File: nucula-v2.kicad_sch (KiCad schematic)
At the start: 7 parts, among them J4 MAIN LINK / OPTIONAL, U9 MCP1700T-3002E/TT

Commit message: Prepare components and JLCPCB BOM for 10-board assembly
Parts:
- C49: LCSC (none) -> C28323; MPN (none) -> CL21B105KBFNNNE; Manufacturer (none) -> Samsung Electro-Mechanics; Tolerance 20% -> 10%; Voltage 10 V -> 50 V
- C50: LCSC (none) -> C19110; MPN (none) -> CL21B225KAFNNNE; Manufacturer (none) -> Samsung Electro-Mechanics; Tolerance 20% -> 10%; Voltage 10 V -> 25 V
- R19, R20: LCSC (none) -> C4190; MPN (none) -> 0603WAF2201T5E; Manufacturer (none) -> UNI-ROYAL(Uniroyal Elec)
- R40: LCSC (none) -> C25803; MPN (none) -> 0603WAF1003T5E; Manufacturer (none) -> UNI-ROYAL(Uniroyal Elec)
- U9: LCSC (none) -> C62244; Manufacturer Microchip -> Microchip Tech
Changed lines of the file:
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@@
       )
     )
-    (property "Manufacturer" "Microchip"
+    (property "Manufacturer" "Microchip Tech"
       (at 66.04 139.7 0)
       (effects
@@
           (unit 1)
         )
+      )
+    )
+    (property "LCSC" "C62244"
+      (at 66.04 139.7 0)
+      (effects
+        (font
+          (size 1.0 1.0)
+        )
+        (hide yes)
       )
     )
@@
       )
     )
-    (property "Datasheet" ""
+    (property "Datasheet" "https://www.lcsc.com/datasheet/lcsc_datasheet_2304140030_Samsung-Electro-Mechanics-CL21B105KBFNNNE_C28323.pdf"
       (at 35.56 160.02 0)
       (effects
@@
       )
     )
-    (property "Voltage" "10 V"
+    (property "Voltage" "50 V"
       (at 35.56 160.02 0)
       (effects
@@
       )
     )
-    (property "Tolerance" "20%"
+    (property "Tolerance" "10%"
       (at 35.56 160.02 0)
       (effects
@@
           (unit 1)
         )
+      )
+    )
+    (property "Manufacturer" "Samsung Electro-Mechanics"
+      (at 35.56 160.02 0)
+      (effects
+        (font
+          (size 1.0 1.0)
+        )
+        (hide yes)
+      )
+    )
+    (property "MPN" "CL21B105KBFNNNE"
+      (at 35.56 160.02 0)
+      (effects
+        (font
+          (size 1.0 1.0)
+        )
+        (hide yes)
+      )
+    )
+    (property "LCSC" "C28323"
+      (at 35.56 160.02 0)
+      (effects
+        (font
+          (size 1.0 1.0)
+        )
+        (hide yes)
       )
     )
@@
       )
     )
-    (property "Datasheet" ""
+    (property "Datasheet" "https://www.lcsc.com/datasheet/lcsc_datasheet_2304140030_Samsung-Electro-Mechanics-CL21B225KAFNNNE_C19110.pdf"
       (at 96.52 160.02 0)
       (effects
@@
       )
     )
-    (property "Voltage" "10 V"
+    (property "Voltage" "25 V"
       (at 96.52 160.02 0)
       (effects
@@
       )
     )
-    (property "Tolerance" "20%"
+    (property "Tolerance" "10%"
       (at 96.52 160.02 0)
       (effects
@@
           (unit 1)
         )
+      )
+    )
+    (property "Manufacturer" "Samsung Electro-Mechanics"
+      (at 96.52 160.02 0)
+      (effects
+        (font
+          (size 1.0 1.0)
+        )
+        (hide yes)
+      )
+    )
+    (property "MPN" "CL21B225KAFNNNE"
+      (at 96.52 160.02 0)
+      (effects
+        (font
+          (size 1.0 1.0)
+        )
+        (hide yes)
+      )
+    )
+    (property "LCSC" "C19110"
+      (at 96.52 160.02 0)
+      (effects
+        (font
+          (size 1.0 1.0)
+        )
+        (hide yes)
       )
     )
@@
       )
     )
-    (property "Datasheet" ""
+    (property "Datasheet" "https://www.lcsc.com/datasheet/lcsc_datasheet_2206010230_UNI-ROYAL-Uniroyal-Elec-0603WAF2201T5E_C4190.pdf"
       (at 142.24 138.43 0)
       (effects
@@
           (unit 1)
         )
+      )
+    )
+    (property "Manufacturer" "UNI-ROYAL(Uniroyal Elec)"
+      (at 142.24 138.43 0)
+      (effects
+        (font
+          (size 1.0 1.0)
+        )
+        (hide yes)
+      )
+    )
+    (property "MPN" "0603WAF2201T5E"
+      (at 142.24 138.43 0)
+      (effects
+        (font
+          (size 1.0 1.0)
+        )
+        (hide yes)
+      )
+    )
+    (property "LCSC" "C4190"
+      (at 142.24 138.43 0)
+      (effects
+        (font
+          (size 1.0 1.0)
+        )
+        (hide yes)
       )
     )
@@
       )
     )
-    (property "Datasheet" ""
+    (property "Datasheet" "https://www.lcsc.com/datasheet/lcsc_datasheet_2206010230_UNI-ROYAL-Uniroyal-Elec-0603WAF2201T5E_C4190.pdf"
       (at 175.26 138.43 0)
       (effects
@@
           (unit 1)
         )
+      )
+    )
+    (property "Manufacturer" "UNI-ROYAL(Uniroyal Elec)"
+      (at 175.26 138.43 0)
+      (effects
+        (font
+          (size 1.0 1.0)
+        )
+        (hide yes)
+      )
+    )
+    (property "MPN" "0603WAF2201T5E"
+      (at 175.26 138.43 0)
+      (effects
+        (font
+          (size 1.0 1.0)
+        )
+        (hide yes)
+      )
+    )
+    (property "LCSC" "C4190"
+      (at 175.26 138.43 0)
+      (effects
+        (font
+          (size 1.0 1.0)
+        )
+        (hide yes)
       )
     )
@@
       )
     )
-    (property "Datasheet" ""
+    (property "Datasheet" "https://www.lcsc.com/datasheet/lcsc_datasheet_2206010045_UNI-ROYAL-Uniroyal-Elec-0603WAF1003T5E_C25803.pdf"
       (at 175.26 172.72 0)
       (effects
@@
       )
     )
+    (property "Manufacturer" "UNI-ROYAL(Uniroyal Elec)"
+      (at 175.26 172.72 0)
+      (effects
+        (font
+          (size 1.0 1.0)
+        )
+        (hide yes)
+      )
+    )
+    (property "MPN" "0603WAF1003T5E"
+      (at 175.26 172.72 0)
+      (effects
+        (font
+          (size 1.0 1.0)
+        )
+        (hide yes)
+      )
+    )
+    (property "LCSC" "C25803"
+      (at 175.26 172.72 0)
+      (effects
+        (font
+          (size 1.0 1.0)
+        )
+        (hide yes)
+      )
+    )

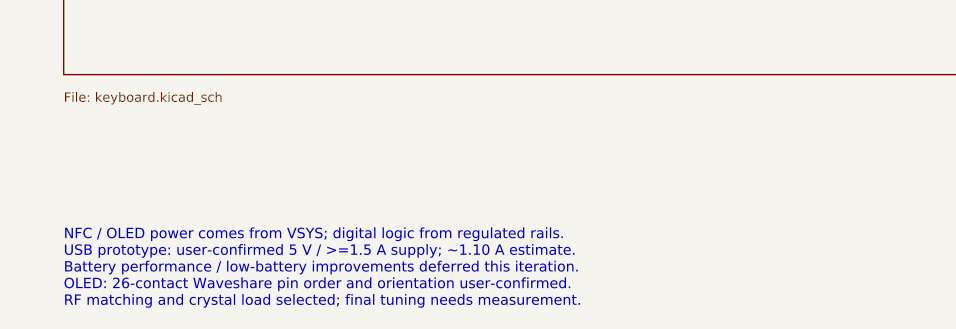
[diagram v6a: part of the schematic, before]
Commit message: Correct OLED interface and routing for 24-pin display
Replace the 26-contact OLED symbol and socket with the verified CON24 pinout and Hirose FH12-24S connector. Preserve DS1 placement and all other board geometry while rerouting its local pad escapes. Update purchasing data, design exports and regression checks.

Validation: zero ERC/DRC errors, no unconnected items or schematic parity issues; 54 layout/regression checks pass; all 261 scoped simulation results unchanged. The two existing U3 silkscreen-edge warnings remain.
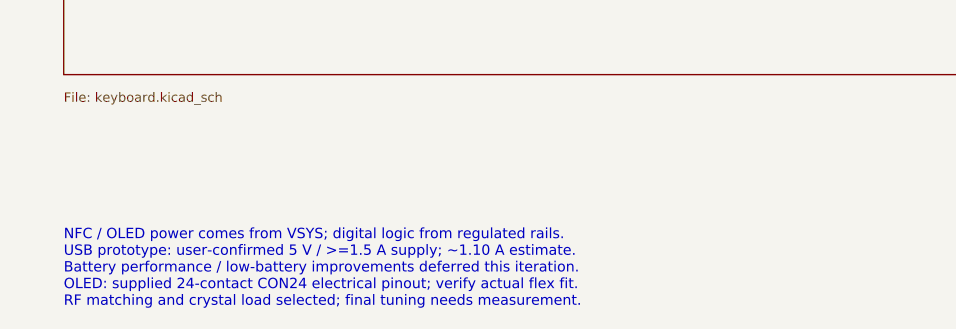
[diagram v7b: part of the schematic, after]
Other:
- note added: "NFC / OLED power comes from VSYS; digital logic from regulated rails. USB prototype: user-confirmed 5 V / >=1.5 A supply; ~1.10 A estimate. Battery performance / low-battery improvements deferred this iteration. OLED: supplied 24-contact CON24 electrical pinout; verify actual flex fit. RF matching and crystal load selected; final tuning needs measurement."
- note removed: "NFC / OLED power comes from VSYS; digital logic from regulated rails. USB prototype: user-confirmed 5 V / >=1.5 A supply; ~1.10 A estimate. Battery performance / low-battery improvements deferred this iteration. OLED: 26-contact Waveshare pin order and orientation user-confirmed. RF matching and crystal load selected; final tuning needs measurement."
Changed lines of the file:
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@@
     )
   )
-  (text "NFC / OLED power comes from VSYS; digital logic from regulated rails.\nUSB prototype: user-confirmed 5 V / >=1.5 A supply; ~1.10 A estimate.\nBattery performance / low-battery improvements deferred this iteration.\nOLED: 26-contact Waveshare pin order and orientation user-confirmed.\nRF matching and crystal load selected; final tuning needs measurement."
+  (text "NFC / OLED power comes from VSYS; digital logic from regulated rails.\nUSB prototype: user-confirmed 5 V / >=1.5 A supply; ~1.10 A estimate.\nBattery performance / low-battery improvements deferred this iteration.\nOLED: supplied 24-contact CON24 electrical pinout; verify actual flex fit.\nRF matching and crystal load selected; final tuning needs measurement."
     (at 20.32 270.51 0)
     (effects
